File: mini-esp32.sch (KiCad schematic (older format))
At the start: 53 parts, among them J1 BAT, J2 USB_B_Micro, J5 Conn_01x18, J6 Conn_01x18, Q1 AO3401A, Q2 S8050, Q3 S8050, Q5 AO3400A, Q6 AO3400A, SW1 RESET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

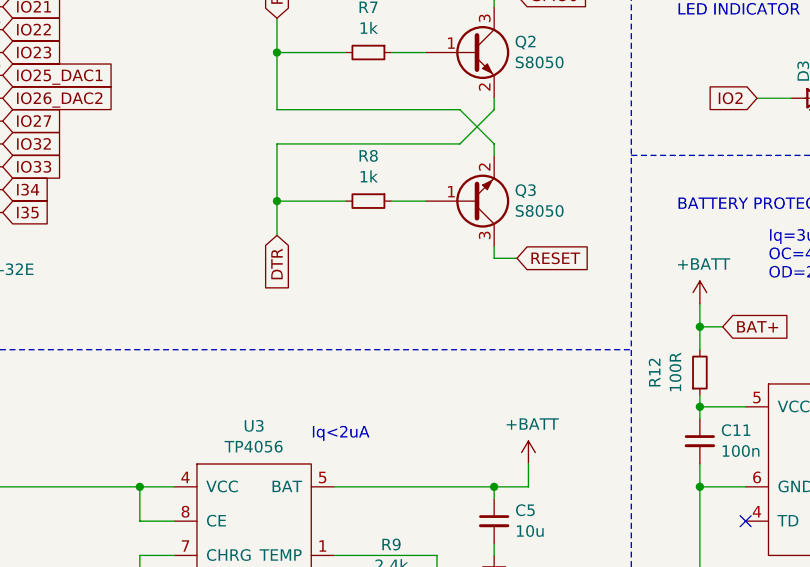
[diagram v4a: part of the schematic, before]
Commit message: Add notes for auto programming circuit
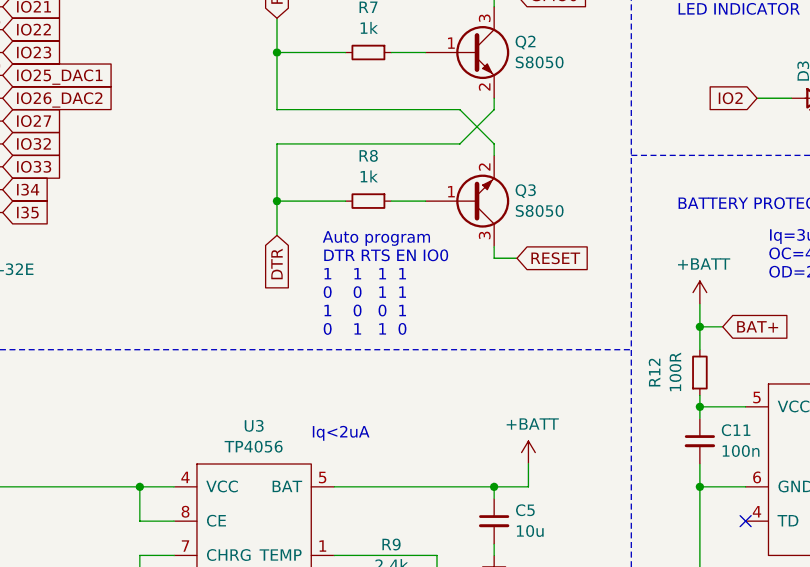
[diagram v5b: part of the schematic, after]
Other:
- note added: "Auto program\nDTR RTS EN IO0\n1 1 1 1\n0 0 1 1\n1 0 0 1\n0 1 1 0"
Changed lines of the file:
@@
 Text Notes 1700 2800 0    50   ~ 0
 VCC = 2.3 - 3.6 V
+Text Notes 3550 5950 0    50   ~ 0
+Auto program\nDTR RTS EN IO0\n1    1   1  1\n0    0   1  1\n1    0   0  1\n0    1   1  0
 $EndSCHEMATC

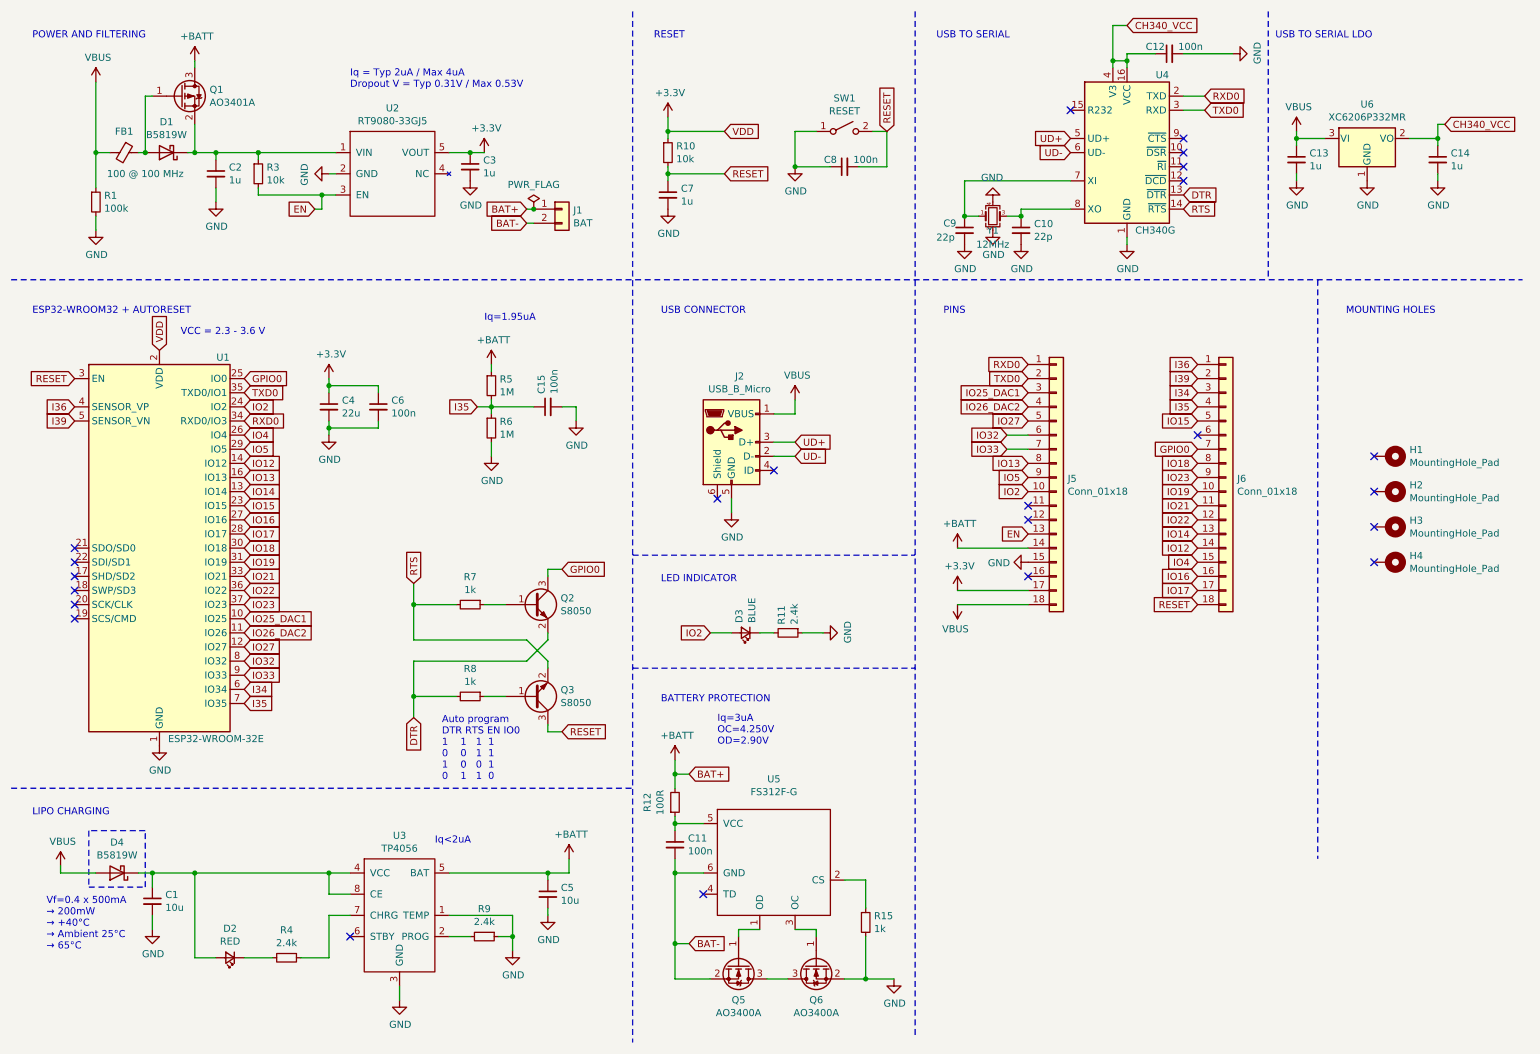
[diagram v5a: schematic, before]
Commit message: Use TPS3839 instead of battery OC/OD. Lower power usage.
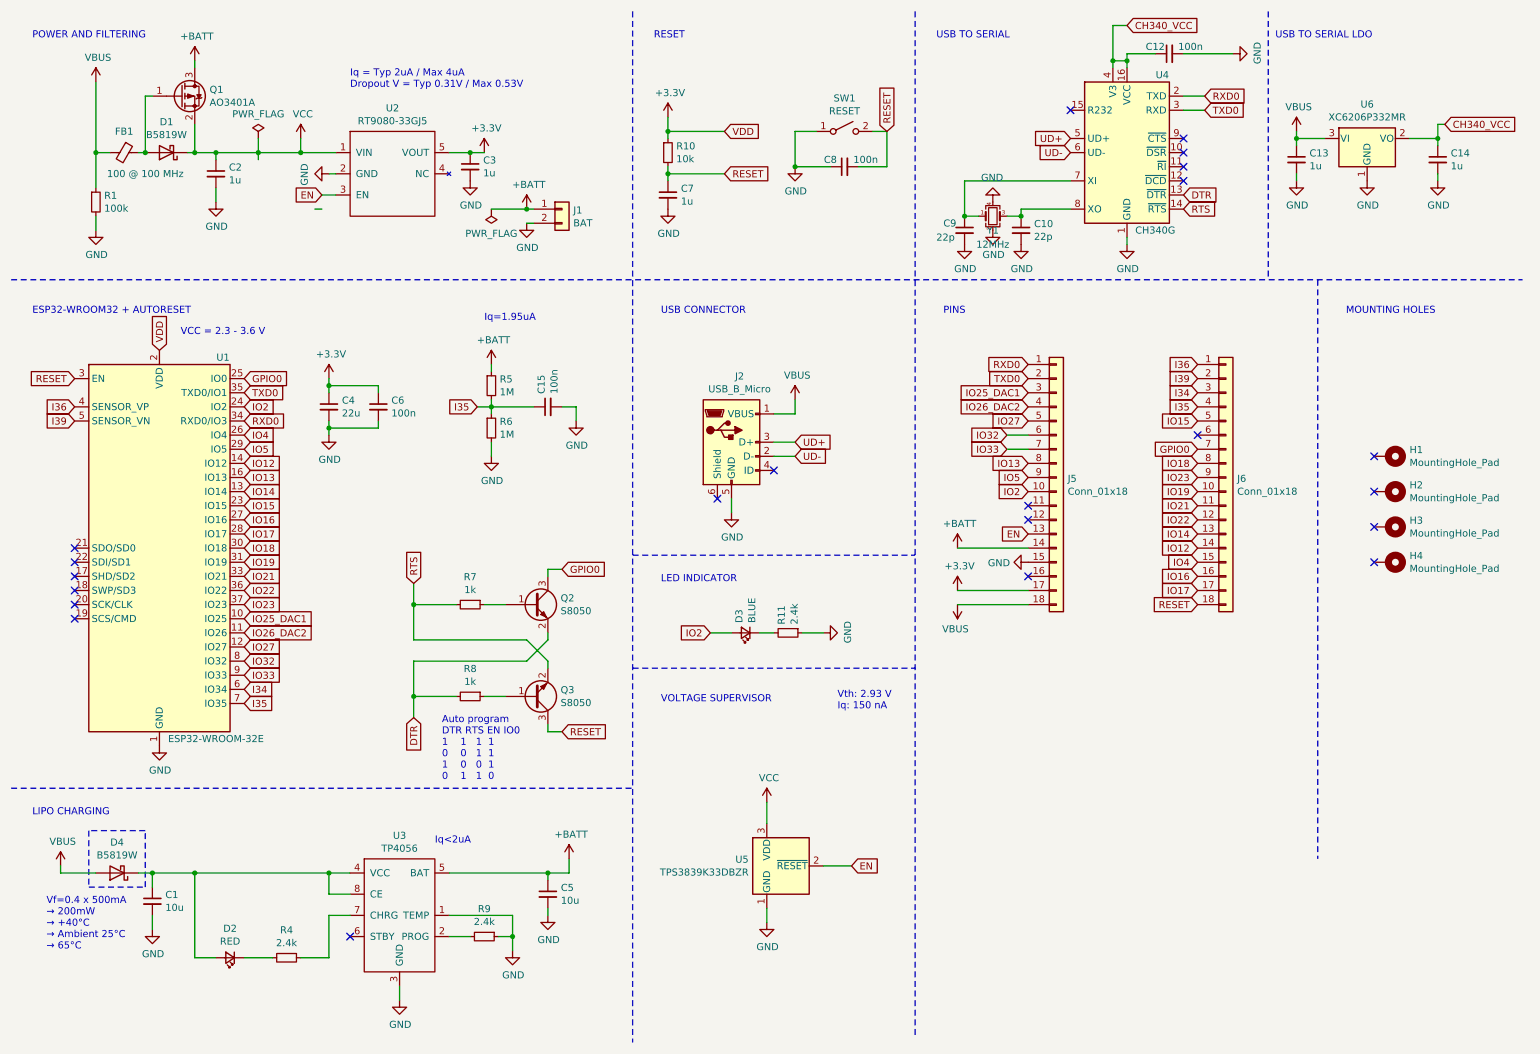
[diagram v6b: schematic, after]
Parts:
- removed C11: 100n, Capacitor_SMD:C_0402_1005Metric, symbol Device:C_Small
- removed Q5, Q6: AO3400A, Package_TO_SOT_SMD:SOT-23, symbol Transistor_FET:AO3400A
- removed R12: 100R, Resistor_SMD:R_0402_1005Metric, symbol Device:R_Small
- removed R15: 1k, Resistor_SMD:R_0402_1005Metric, symbol Device:R_Small
- removed R3: 10k, Resistor_SMD:R_0402_1005Metric, symbol Device:R_Small
- removed U5: FS312F-G, Package_TO_SOT_SMD:SOT-23-6, symbol myLib:FS312F-G
- added U5: TPS3839K33DBZR, Package_TO_SOT_SMD:SOT-23, symbol Power_Supervisor:TPS3839DBZ
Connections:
- net BAT- is gone; now on net GND: J1.2 (Pin_2)
- net EN: now also U5.2 (~RESET)
- net GND: now also U5.1 (GND)
- net VCC: now reaches C2.1, D1.1 (K), Q1.2 (S), U2.1 (VIN)
- net VCC: now also U5.3 (VDD)
- no-connect marks 23 -> 22
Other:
- note added: "VOLTAGE SUPERVISOR"
- note added: "Vth: 2.93 V\nIq: 150 nA"
- note removed: "BATTERY PROTECTION"
- note removed: "Iq=3uA\nOC=4.250V\nOD=2.90V"
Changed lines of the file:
@@
 Title "Mini ESP32"
 Date "2020-10-11"
-Rev "3.0.1"
+Rev "4.0"
 Comp ""
 Comment1 ""
@@
 Wire Wire Line
 	1800 900  1800 850
-Text GLabel 2650 1900 0    50   Input ~ 0
+Text GLabel 2700 1800 0    50   Input ~ 0
 EN
-Wire Wire Line
-	2650 1900 2700 1900
-Wire Wire Line
-	2700 1900 2700 1800
-Connection ~ 2700 1800
-Wire Wire Line
-	2700 1800 2250 1800
 $Comp
 L Connector_Generic:Conn_01x02 J1
@@
 Wire Wire Line
 	1100 1000 1100 1500
-$Comp
-L power:+BATT #PWR0107
-U 1 1 5FBE7D4B
-P 5200 5800
-F 0 "#PWR0107" H 5200 5650 50  0001 C CNN
-F 1 "+BATT" H 5215 5973 50  0000 C CNN
-F 2 "" H 5200 5800 50  0001 C CNN
-F 3 "" H 5200 5800 50  0001 C CNN
-	1    5200 5800
-	1    0    0    -1
-$EndComp
-Wire Wire Line
-	5200 6600 5400 6600
-$Comp
-L Transistor_FET:AO3400A Q6
-U 1 1 5FBFA0D1
-P 6200 7250
-F 0 "Q6" V 6449 7250 50  0000 C CNN
-F 1 "AO3400A" V 6540 7250 50  0000 C CNN
-F 2 "Package_TO_SOT_SMD:SOT-23" H 6400 7175 50  0001 L CIN
-F 3 "http://www.aosmd.com/pdfs/datasheet/AO3400A.pdf" H 6200 7250 50  0001 L CNN
-F 4 "C20917" H 6200 7250 50  0001 C CNN "LCSC Part #"
-	1    6200 7250
-	0    -1   1    0
-$EndComp
-Wire Wire Line
-	5850 7350 6000 7350
-$Comp
-L Transistor_FET:AO3400A Q5
-U 1 1 5FBF3F7C
-P 5650 7250
-F 0 "Q5" V 5899 7250 50  0000 C CNN
-F 1 "AO3400A" V 5990 7250 50  0000 C CNN
-F 2 "Package_TO_SOT_SMD:SOT-23" H 5850 7175 50  0001 L CIN
-F 3 "http://www.aosmd.com/pdfs/datasheet/AO3400A.pdf" H 5650 7250 50  0001 L CNN
-F 4 "C20917" H 5650 7250 50  0001 C CNN "LCSC Part #"
-	1    5650 7250
-	0    1    1    0
-$EndComp
-Wire Wire Line
-	5650 7050 5650 7000
-Wire Wire Line
-	6200 7050 6200 7000
-Wire Wire Line
-	6750 7350 6550 7350
-$Comp
-L Device:R_Small R15
-U 1 1 5FC2A966
-P 6550 6950
-F 0 "R15" H 6609 6996 50  0000 L CNN
-F 1 "1k" H 6609 6905 50  0000 L CNN
-F 2 "Resistor_SMD:R_0402_1005Metric" H 6550 6950 50  0001 C CNN
-F 3 "~" H 6550 6950 50  0001 C CNN
-F 4 "C11702" H 6550 6950 50  0001 C CNN "LCSC Part #"
-	1    6550 6950
-	1    0    0    -1
-$EndComp
-$Comp
-L myLib:FS312F-G U5
-U 1 1 5FBE4449
-P 5900 6000
-F 0 "U5" H 5900 6065 50  0000 C CNN
-F 1 "FS312F-G" H 5900 5974 50  0000 C CNN
-F 2 "Package_TO_SOT_SMD:SOT-23-6" H 5900 6000 50  0001 C CNN
-F 3 "" H 5900 6000 50  0001 C CNN
-F 4 "C82736" H 5900 6000 50  0001 C CNN "LCSC Part #"
-	1    5900 6000
-	1    0    0    -1
-$EndComp
-Wire Wire Line
-	6550 7050 6550 7350
-Connection ~ 6550 7350
-Wire Wire Line
-	6550 7350 6400 7350
-Wire Wire Line
-	5200 7350 5200 7100
-$Comp
-L Device:C_Small C11
-U 1 1 5FC424C5
-P 5200 6400
-F 0 "C11" H 5292 6446 50  0000 L CNN
-F 1 "100n" H 5292 6355 50  0000 L CNN
-F 2 "Capacitor_SMD:C_0402_1005Metric" H 5200 6400 50  0001 C CNN
-F 3 "~" H 5200 6400 50  0001 C CNN
-F 4 "C1525" H 5200 6400 50  0001 C CNN "LCSC Part #"
-	1    5200 6400
-	1    0    0    -1
-$EndComp
-Wire Wire Line
-	5200 6300 5200 6250
-Wire Wire Line
-	5200 6600 5200 6500
-Connection ~ 5200 6600
 Wire Wire Line
 	6100 4900 6250 4900
@@
 	-1   0    0    1
 $EndComp
-Text GLabel 4150 1900 0    50   Input ~ 0
-BAT+
-Wire Wire Line
-	4150 2000 4200 2000
-Wire Wire Line
-	4150 1900 4200 1900
-Text GLabel 5300 5900 2    50   Input ~ 0
-BAT+
-Wire Wire Line
-	5300 5900 5200 5900
-Wire Wire Line
-	5200 5900 5200 5800
-Text GLabel 5300 7100 2    50   Input ~ 0
-BAT-
-Wire Wire Line
-	5300 7100 5200 7100
-Connection ~ 5200 7100
-Wire Wire Line
-	5200 7100 5200 6600
-$Comp
-L power:GND #PWR0108
-U 1 1 5FCB8A37
-P 6750 7350
-F 0 "#PWR0108" H 6750 7100 50  0001 C CNN
-F 1 "GND" H 6755 7177 50  0000 C CNN
-F 2 "" H 6750 7350 50  0001 C CNN
-F 3 "" H 6750 7350 50  0001 C CNN
-	1    6750 7350
-	1    0    0    -1
-$EndComp
 Text Notes 5100 5400 0    50   ~ 0
-BATTERY PROTECTION
+VOLTAGE SUPERVISOR
 Wire Notes Line
 	4900 5150 6900 5150
 Wire Wire Line
-	5450 7350 5200 7350
-Wire Wire Line
-	5650 7000 5800 7000
-Wire Wire Line
-	6050 7000 6200 7000
-Wire Wire Line
-	6400 6650 6550 6650
-Wire Wire Line
-	6550 6650 6550 6850
-Text GLabel 4150 2000 0    50   Input ~ 0
-BAT-
-Wire Wire Line
 	8800 1200 8950 1200
 Wire Wire Line
 	1950 1500 2250 1500
-$Comp
-L Device:R_Small R3
-U 1 1 5FB3AA5C
-P 2250 1650
-F 0 "R3" H 2309 1696 50  0000 L CNN
-F 1 "10k" H 2309 1605 50  0000 L CNN
-F 2 "Resistor_SMD:R_0402_1005Metric" H 2250 1650 50  0001 C CNN
-F 3 "~" H 2250 1650 50  0001 C CNN
-F 4 "C25744" H 2250 1650 50  0001 C CNN "LCSC Part #"
-	1    2250 1650
-	1    0    0    -1
-$EndComp
 Wire Wire Line
 	2250 1550 2250 1500
 Connection ~ 2250 1500
 Wire Wire Line
-	2250 1500 2800 1500
-Wire Wire Line
-	2250 1750 2250 1800
-Wire Wire Line
 	3850 5350 4000 5350
 Wire Wire Line
 	3850 4700 4000 4700
-NoConn ~ 5400 6750
-$Comp
-L Device:R_Small R12
-U 1 1 5FBAC8E8
-P 5200 6100
-F 0 "R12" V 5004 6100 50  0000 C CNN
-F 1 "100R" V 5095 6100 50  0000 C CNN
-F 2 "Resistor_SMD:R_0402_1005Metric" H 5200 6100 50  0001 C CNN
-F 3 "~" H 5200 6100 50  0001 C CNN
-F 4 "C25076" H 5200 6100 50  0001 C CNN "LCSC Part #"
-	1    5200 6100
-	1    0    0    1
-$EndComp
-Wire Wire Line
-	5200 5900 5200 6000
-Connection ~ 5200 5900
 Wire Notes Line
 	4900 500  4900 7800
-Wire Wire Line
-	5400 6250 5200 6250
-Connection ~ 5200 6250
-Wire Wire Line
-	5200 6250 5200 6200
 Connection ~ 10600 1400
 Wire Wire Line
@@
 	8800 800  9150 800
 $Comp
-L power:PWR_FLAG #FLG0101
-U 1 1 5FC5E9DE
-P 4200 1900
-F 0 "#FLG0101" H 4200 1975 50  0001 C CNN
-F 1 "PWR_FLAG" H 4200 2073 50  0000 C CNN
-F 2 "" H 4200 1900 50  0001 C CNN
-F 3 "~" H 4200 1900 50  0001 C CNN
-	1    4200 1900
-	1    0    0    -1
-$EndComp
-Connection ~ 4200 1900
-$Comp
 L Device:D_Schottky D4
 U 1 1 5FCD5A57
@@
 Text Notes 750  7150 0    50   ~ 0
 Vf=0.4 x 500mA\n→ 200mW\n→ +40°C\n→ Ambient 25°C\n→ 65°C
-Text Notes 5500 5700 0    50   ~ 0
-Iq=3uA\nOC=4.250V\nOD=2.90V
+Text Notes 6350 5450 0    50   ~ 0
+Vth: 2.93 V\nIq: 150 nA
 Wire Notes Line
 	1050 6300 1050 6700
@@
 Text Notes 3550 5950 0    50   ~ 0
 Auto program\nDTR RTS EN IO0\n1    1   1  1\n0    0   1  1\n1    0   0  1\n0    1   1  0
+$Comp
+L power:GND #PWR0107
+U 1 1 5FBEE08C
+P 4150 2000
+F 0 "#PWR0107" H 4150 1750 50  0001 C CNN
+F 1 "GND" H 4155 1827 50  0000 C CNN
+F 2 "" H 4150 2000 50  0001 C CNN
+F 3 "" H 4150 2000 50  0001 C CNN
+	1    4150 2000
+	1    0    0    -1
+$EndComp
+$Comp
+L power:+BATT #PWR0108
+U 1 1 5FBEE4D3
+P 4150 1900
+F 0 "#PWR0108" H 4150 1750 50  0001 C CNN
+F 1 "+BATT" H 4165 2073 50  0000 C CNN
+F 2 "" H 4150 1900 50  0001 C CNN
+F 3 "" H 4150 1900 50  0001 C CNN
+	1    4150 1900
+	1    0    0    -1
+$EndComp
+Wire Wire Line
+	4150 1900 4200 1900
+Wire Wire Line
+	4150 2000 4200 2000
+$Comp
+L Power_Supervisor:TPS3839DBZ U5
+U 1 1 5FC2BC90
+P 5850 6550
+F 0 "U5" H 5721 6596 50  0000 R CNN
+F 1 "TPS3839K33DBZR" H 5721 6505 50  0000 R CNN
+F 2 "Package_TO_SOT_SMD:SOT-23" H 5850 6550 50  0001 C CNN
+F 3 "http://www.ti.com/lit/ds/sbvs193d/sbvs193d.pdf" H 5850 6550 50  0001 C CNN
+F 4 "C96333" H 5850 6550 50  0001 C CNN "LCSC Part #"
+	1    5850 6550
+	1    0    0    -1
+$EndComp
+Wire Wire Line
+	2250 1500 2550 1500
+$Comp
+L power:VCC #PWR0116
+U 1 1 5FC2F87D
+P 2550 1400
+F 0 "#PWR0116" H 2550 1250 50  0001 C CNN
+F 1 "VCC" H 2565 1573 50  0000 C CNN
+F 2 "" H 2550 1400 50  0001 C CNN
+F 3 "" H 2550 1400 50  0001 C CNN
+	1    2550 1400
+	1    0    0    -1
+$EndComp
+Wire Wire Line
+	2550 1500 2550 1400
+Connection ~ 2550 1500
+Wire Wire Line
+	2550 1500 2800 1500
+$Comp
+L power:VCC #PWR0117
+U 1 1 5FC34DE1
+P 5850 6100
+F 0 "#PWR0117" H 5850 5950 50  0001 C CNN
+F 1 "VCC" H 5865 6273 50  0000 C CNN
+F 2 "" H 5850 6100 50  0001 C CNN
+F 3 "" H 5850 6100 50  0001 C CNN
+	1    5850 6100
+	1    0    0    -1
+$EndComp
+$Comp
+L power:GND #PWR0122
+U 1 1 5FC40CF3
+P 5850 6950
+F 0 "#PWR0122" H 5850 6700 50  0001 C CNN
+F 1 "GND" H 5855 6777 50  0000 C CNN
+F 2 "" H 5850 6950 50  0001 C CNN
+F 3 "" H 5850 6950 50  0001 C CNN
+	1    5850 6950
+	1    0    0    -1
+$EndComp
+Wire Wire Line
+	5850 6950 5850 6850
+$Comp
+L power:PWR_FLAG #FLG0101
+U 1 1 5FC47EE1
+P 3900 1900
+F 0 "#FLG0101" H 3900 1975 50  0001 C CNN
+F 1 "PWR_FLAG" H 3900 2073 50  0000 C CNN
+F 2 "" H 3900 1900 50  0001 C CNN
+F 3 "~" H 3900 1900 50  0001 C CNN
+	1    3900 1900
+	-1   0    0    1
+$EndComp
+Wire Wire Line
+	3900 1900 4150 1900
+Connection ~ 4150 1900
+$Comp
+L power:PWR_FLAG #FLG0102
+U 1 1 5FC4EDFC
+P 2250 1400
+F 0 "#FLG0102" H 2250 1475 50  0001 C CNN
+F 1 "PWR_FLAG" H 2250 1573 50  0000 C CNN
+F 2 "" H 2250 1400 50  0001 C CNN
+F 3 "~" H 2250 1400 50  0001 C CNN
+	1    2250 1400
+	1    0    0    -1
+$EndComp
+Wire Wire Line
+	2250 1400 2250 1500
+Wire Wire Line
+	6450 6550 6250 6550
+Text GLabel 6450 6550 2    50   Input ~ 0
+EN
+Wire Wire Line
+	5850 6100 5850 6250
+Wire Wire Line
+	2650 1900 2700 1900
 $EndSCHEMATC
